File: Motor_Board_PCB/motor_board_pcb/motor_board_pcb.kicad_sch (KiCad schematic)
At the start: 13 parts, among them U1 MCP2515-xST, U2 TJA1050, Y1 20M

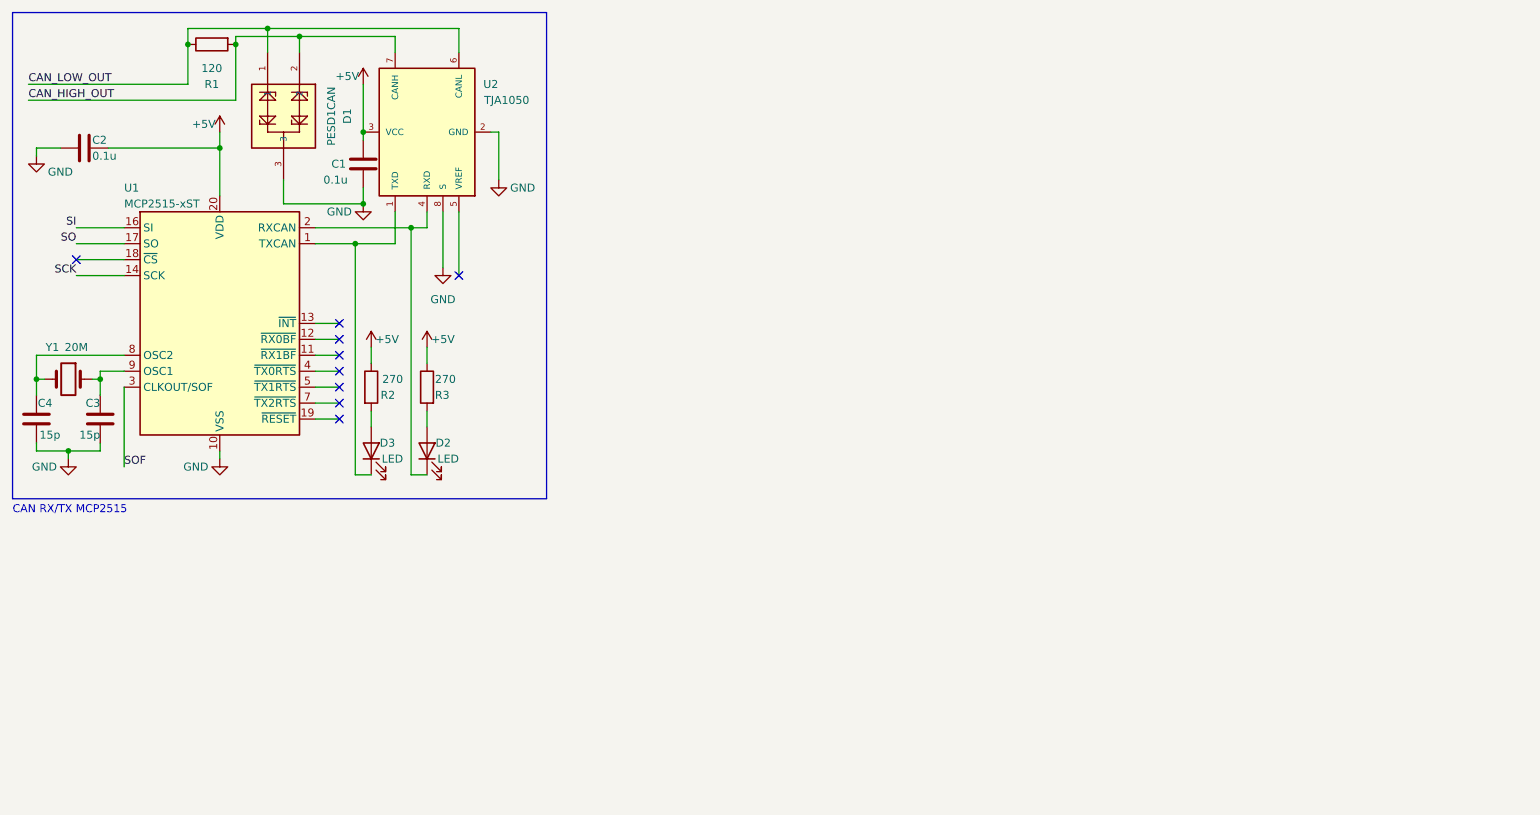
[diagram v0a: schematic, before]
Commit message: added MCU sheet to motor driver schematic
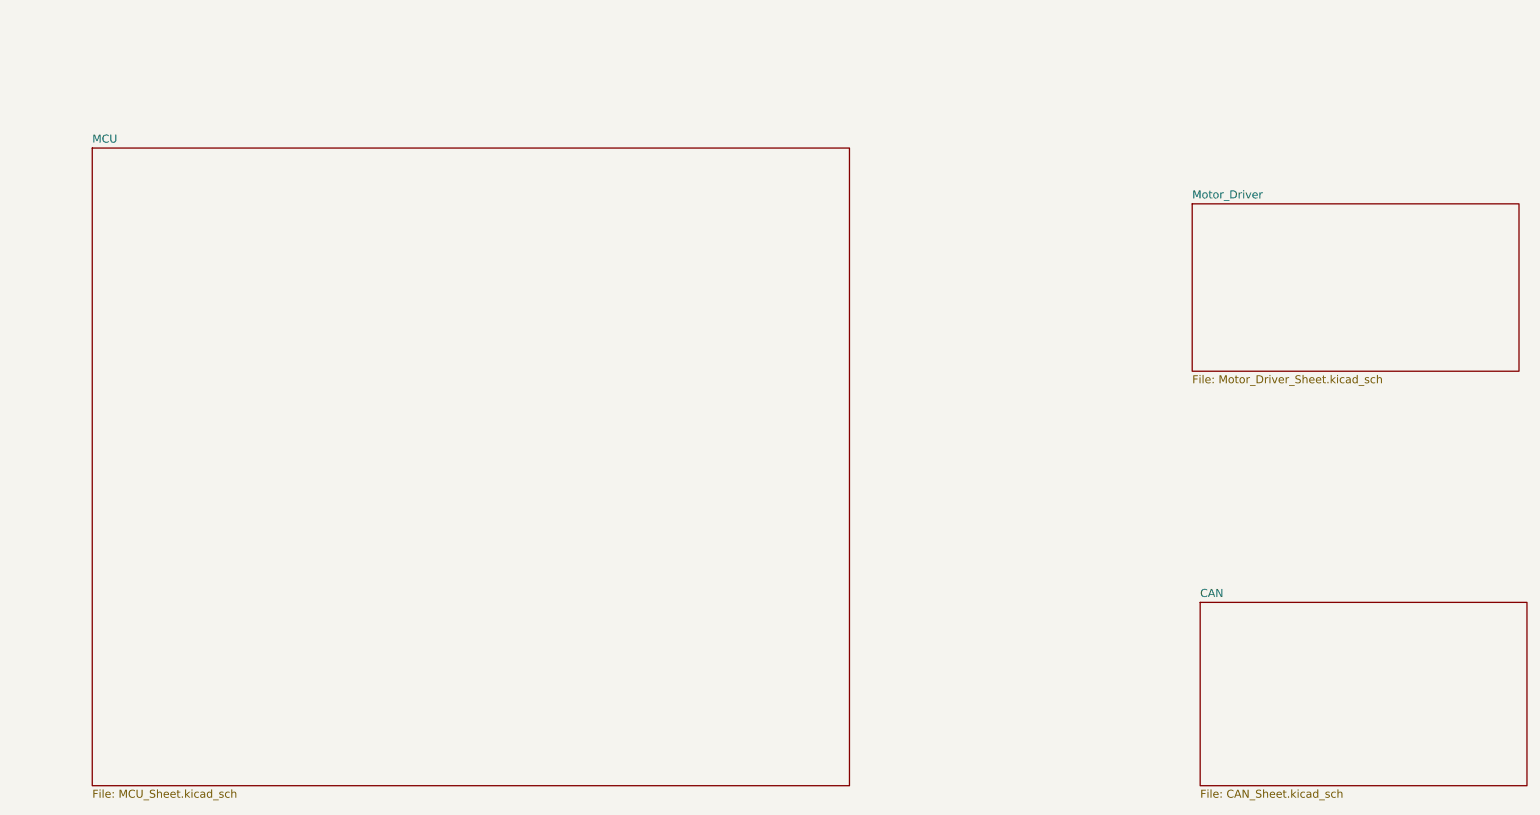
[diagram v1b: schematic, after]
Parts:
- removed C1, C2: 0.1u, Capacitor_SMD:C_0603_1608Metric, symbol Device:C
- removed C3, C4: 15p, Capacitor_SMD:C_0603_1608Metric, symbol Device:C
- removed D1: PESD1CAN, PESD1CAN:SOT23-3, symbol PESD1CAN:PESD1CAN
- removed D2, D3: LED, LED_SMD:LED_1206_3216Metric, symbol Device:LED
- removed R1: 120, Resistor_SMD:R_0603_1608Metric_Pad0.98x0.95mm_HandSolder, symbol Device:R
- removed R2, R3: 270, Resistor_SMD:R_0603_1608Metric_Pad0.98x0.95mm_HandSolder, symbol Device:R
- removed U1: MCP2515-xST, Package_SO:TSSOP-20_4.4x6.5mm_P0.65mm, symbol Interface_CAN_LIN:MCP2515-xST
- removed U2: TJA1050, TJA1050:SOT96-1, symbol TJA1050:TJA1050
- removed Y1: 20M, Crystal:Crystal_HC49-U_Vertical, symbol Device:Crystal
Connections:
- no-connect marks 9 -> 0
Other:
- added sheet CAN (CAN_Sheet.kicad_sch)
- added sheet MCU (MCU_Sheet.kicad_sch)
- added sheet Motor_Driver (Motor_Driver_Sheet.kicad_sch)
- note removed: "CAN RX/TX MCP2515"
